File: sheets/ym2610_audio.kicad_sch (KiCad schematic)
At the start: 56 parts, among them J3 SMK S-G8043, Q101 2SC1815, Q102 2SC1815, U26 YM3016D, U27 YM2610, U28 PC4741, U29 PC4741

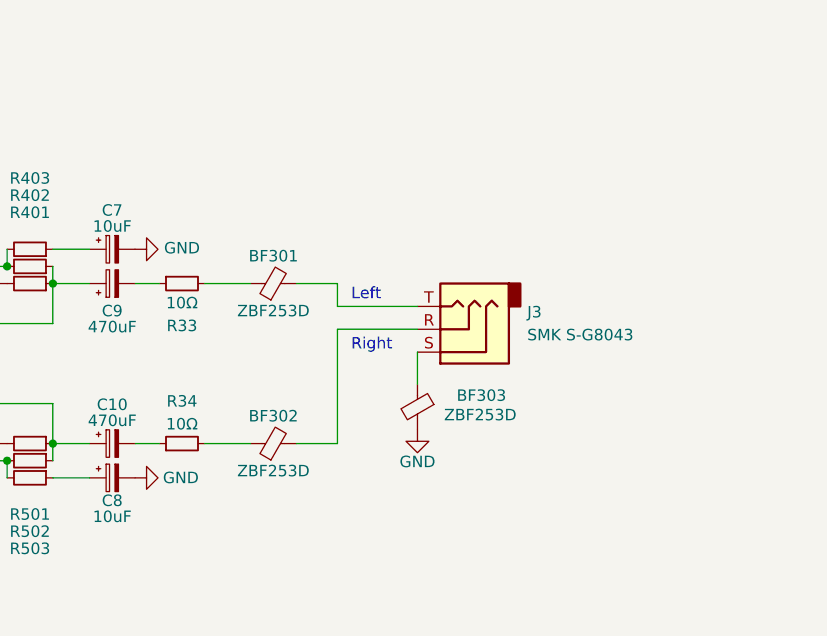
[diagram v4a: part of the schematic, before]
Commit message: Put Resistor Back, Swap Headphone
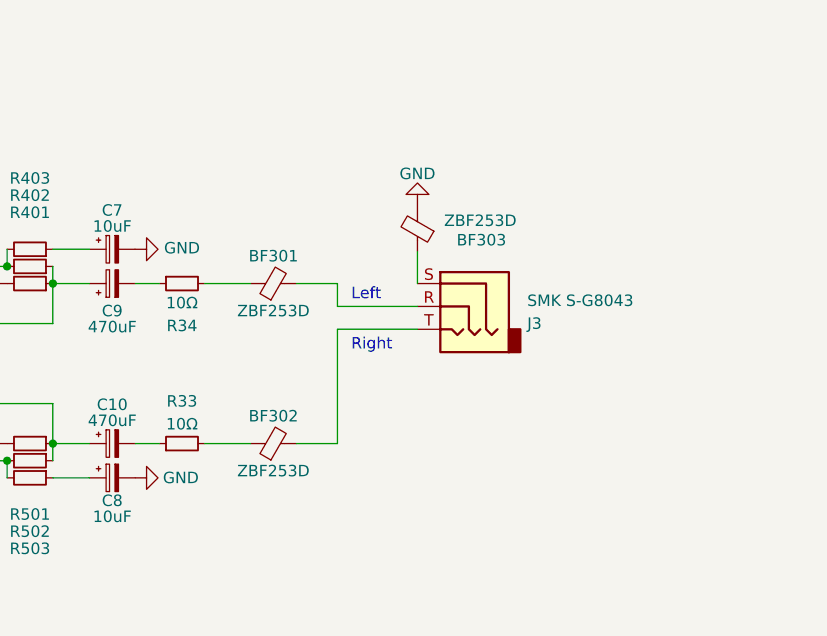
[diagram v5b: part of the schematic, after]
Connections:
- net at C9.2: now also R34.1; no longer R33.1
- net at BF301.1: now also R34.2; no longer R33.2
- net at BF301.2: now also J3.R; no longer J3.T
- net at C10.2: now also R33.1; no longer R34.1
- net at BF302.1: now also R33.2; no longer R34.2
- net at BF302.2: now also J3.T; no longer J3.R
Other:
- moved on the sheet: BF303, J3, R33, R34
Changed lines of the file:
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@@
     (stroke (width 0) (type default) (color 0 0 0 0))
   )
-  (wire (pts (xy 265.938 216.408) (xy 265.938 219.964))
+  (wire (pts (xy 265.938 205.232) (xy 265.938 208.788))
     (stroke (width 0) (type default) (color 0 0 0 0))
   )
@@
     (pin "2")
   )
-  (symbol (lib_id "Device:FerriteBead_Small") (at 265.938 222.504 0) (mirror y) (unit 1)
-    (in_bom yes) (on_board yes)
-    (property "Reference" "BF303" (id 0) (at 273.05 221.234 0))
-    (property "Value" "ZBF253D" (id 1) (at 272.923 223.393 0))
-    (property "Footprint" "1_NeoGeoLibrary:BF-2.5mm" (id 2) (at 267.716 222.504 90)
-      (effects (font (size 1.27 1.27)) hide)
-    )
-    (property "Datasheet" "" (id 3) (at 265.938 222.504 0)
+  (symbol (lib_id "Device:FerriteBead_Small") (at 265.938 202.692 180) (unit 1)
+    (in_bom yes) (on_board yes)
+    (property "Reference" "BF303" (id 0) (at 273.05 203.962 0))
+    (property "Value" "ZBF253D" (id 1) (at 272.923 201.803 0))
+    (property "Footprint" "1_NeoGeoLibrary:BF-2.5mm" (id 2) (at 267.716 202.692 90)
+      (effects (font (size 1.27 1.27)) hide)
+    )
+    (property "Datasheet" "" (id 3) (at 265.938 202.692 0)
       (effects (font (size 1.27 1.27)) hide)
     )
@@
     (pin "2")
   )
-  (symbol (lib_id "power:GND") (at 265.938 225.044 0) (mirror y) (unit 1)
-    (in_bom yes) (on_board yes)
-    (property "Reference" "#PWR0193" (id 0) (at 265.938 231.394 0)
-      (effects (font (size 1.27 1.27)) hide)
-    )
-    (property "Value" "GND" (id 1) (at 265.938 228.6 0))
-    (property "Footprint" "" (id 2) (at 265.938 225.044 0)
-      (effects (font (size 1.27 1.27)) hide)
-    )
-    (property "Datasheet" "" (id 3) (at 265.938 225.044 0)
+  (symbol (lib_id "power:GND") (at 265.938 200.152 180) (unit 1)
+    (in_bom yes) (on_board yes)
+    (property "Reference" "#PWR0193" (id 0) (at 265.938 193.802 0)
+      (effects (font (size 1.27 1.27)) hide)
+    )
+    (property "Value" "GND" (id 1) (at 265.938 196.596 0))
+    (property "Footprint" "" (id 2) (at 265.938 200.152 0)
+      (effects (font (size 1.27 1.27)) hide)
+    )
+    (property "Datasheet" "" (id 3) (at 265.938 200.152 0)
       (effects (font (size 1.27 1.27)) hide)
     )
@@
     (pin "1")
   )
-  (symbol (lib_id "Device:R_Small") (at 239.776 208.788 90) (mirror x) (unit 1)
-    (in_bom yes) (on_board yes)
-    (property "Reference" "R33" (id 0) (at 239.776 213.487 90))
-    (property "Value" "10Ω" (id 1) (at 239.776 210.947 90))
-    (property "Footprint" "Resistor_THT:R_Axial_DIN0207_L6.3mm_D2.5mm_P10.16mm_Horizontal" (id 2) (at 239.776 208.788 0)
-      (effects (font (size 1.27 1.27)) hide)
-    )
-    (property "Datasheet" "" (id 3) (at 239.776 208.788 0)
+  (symbol (lib_id "Device:R_Small") (at 239.776 226.568 90) (unit 1)
+    (in_bom yes) (on_board yes)
+    (property "Reference" "R33" (id 0) (at 239.776 221.869 90))
+    (property "Value" "10Ω" (id 1) (at 239.776 224.409 90))
+    (property "Footprint" "Resistor_THT:R_Axial_DIN0207_L6.3mm_D2.5mm_P10.16mm_Horizontal" (id 2) (at 239.776 226.568 0)
+      (effects (font (size 1.27 1.27)) hide)
+    )
+    (property "Datasheet" "" (id 3) (at 239.776 226.568 0)
       (effects (font (size 1.27 1.27)) hide)
     )
@@
     (pin "2")
   )
-  (symbol (lib_id "Device:R_Small") (at 239.776 226.568 90) (unit 1)
-    (in_bom yes) (on_board yes)
-    (property "Reference" "R34" (id 0) (at 239.776 221.869 90))
-    (property "Value" "10Ω" (id 1) (at 239.776 224.409 90))
-    (property "Footprint" "Resistor_THT:R_Axial_DIN0207_L6.3mm_D2.5mm_P10.16mm_Horizontal" (id 2) (at 239.776 226.568 0)
-      (effects (font (size 1.27 1.27)) hide)
-    )
-    (property "Datasheet" "" (id 3) (at 239.776 226.568 0)
+  (symbol (lib_id "Device:R_Small") (at 239.776 208.788 90) (mirror x) (unit 1)
+    (in_bom yes) (on_board yes)
+    (property "Reference" "R34" (id 0) (at 239.776 213.487 90))
+    (property "Value" "10Ω" (id 1) (at 239.776 210.947 90))
+    (property "Footprint" "Resistor_THT:R_Axial_DIN0207_L6.3mm_D2.5mm_P10.16mm_Horizontal" (id 2) (at 239.776 208.788 0)
+      (effects (font (size 1.27 1.27)) hide)
+    )
+    (property "Datasheet" "" (id 3) (at 239.776 208.788 0)
       (effects (font (size 1.27 1.27)) hide)
     )
@@
     (pin "2")
   )
-  (symbol (lib_id "Connector:AudioJack3") (at 271.018 213.868 180) (unit 1)
+  (symbol (lib_id "Connector:AudioJack3") (at 271.018 211.328 0) (mirror y) (unit 1)
     (in_bom yes) (on_board yes) (fields_autoplaced)
-    (property "Reference" "J3" (id 0) (at 278.13 211.9629 0)
+    (property "Reference" "J3" (id 0) (at 278.13 213.2331 0)
       (effects (font (size 1.27 1.27)) (justify right))
     )
-    (property "Value" "SMK S-G8043" (id 1) (at 278.13 214.5029 0)
+    (property "Value" "SMK S-G8043" (id 1) (at 278.13 210.6931 0)
       (effects (font (size 1.27 1.27)) (justify right))
     )
-    (property "Footprint" "1_NeoGeoLibrary:J3" (id 2) (at 271.018 213.868 0)
-      (effects (font (size 1.27 1.27)) hide)
-    )
-    (property "Datasheet" "~" (id 3) (at 271.018 213.868 0)
-      (effects (font (size 1.27 1.27)) hide)
-    )
+    (property "Footprint" "1_NeoGeoLibrary:J3" (id 2) (at 271.018 211.328 0)
+      (effects (font (size 1.27 1.27)) hide)
+    )
+    (property "Datasheet" "~" (id 3) (at 271.018 211.328 0)
+      (effects (font (size 1.27 1.27)) hide)
+    )

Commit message: Merged From Stable
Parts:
- RV1: footprint 1_NeoGeoLibrary:Volume-Slider -> 1_NeoGeoLibrary:RV1
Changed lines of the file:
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@@
       (effects (font (size 1.27 1.27)) (justify right))
     )
-    (property "Footprint" "1_NeoGeoLibrary:Volume-Slider" (id 2) (at 59.563 211.328 0)
+    (property "Footprint" "1_NeoGeoLibrary:RV1" (id 2) (at 59.563 211.328 0)
       (effects (font (size 1.27 1.27)) hide)
     )

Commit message: Upgrade Schematics to Kicad 7.0
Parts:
- J3: symbol Connector:AudioJack3 -> Connector_Audio:AudioJack3

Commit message: Updated footprints from PCB to Schematics
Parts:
- R33, R34: footprint Resistor_THT:R_Axial_DIN0207_L6.3mm_D2.5mm_P10.16mm_Horizontal -> 1_NeoGeoLibrary:R76
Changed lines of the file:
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@@
       (effects (font (size 1.27 1.27)))
     )
-    (property "Footprint" "Resistor_THT:R_Axial_DIN0207_L6.3mm_D2.5mm_P10.16mm_Horizontal" (at 239.776 226.568 0)
+    (property "Footprint" "1_NeoGeoLibrary:R76" (at 239.776 226.568 0)
       (effects (font (size 1.27 1.27)) hide)
     )
@@
       (effects (font (size 1.27 1.27)))
     )
-    (property "Footprint" "Resistor_THT:R_Axial_DIN0207_L6.3mm_D2.5mm_P10.16mm_Horizontal" (at 239.776 208.788 0)
+    (property "Footprint" "1_NeoGeoLibrary:R76" (at 239.776 208.788 0)
       (effects (font (size 1.27 1.27)) hide)
     )
